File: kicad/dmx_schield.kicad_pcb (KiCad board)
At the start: 2 copper layers, 101.6 x 78.7 mm, 103 parts, among them J1 Conn_01x17, J2 Conn_01x17, J250 Conn_01x01, J251 Conn_01x01, J30 Conn_01x04, J40 Conn_01x06, J41 Conn_01x01, J42 Conn_01x01, J43 Conn_01x01, J50 Conn_01x02, J60 Conn_01x03, Q1 BSR14, Q50 IRLML5203, SW1 SW_Push, SW2 SW_Push, SW3 SW_Push, SW4 SW_Push, U1 DCDC-SIP8-1-2-(3)-6-7, U11 DCDC-SIP7-1-2-4-6, U140 LM317_3PinPackage, U3 LTV-847S, U5 LTV-827S, U6 ADUM1301, U60 MAX481E, U61 74LVC2G34, U7 REE-0505S/1S7E_0505S1.5UP

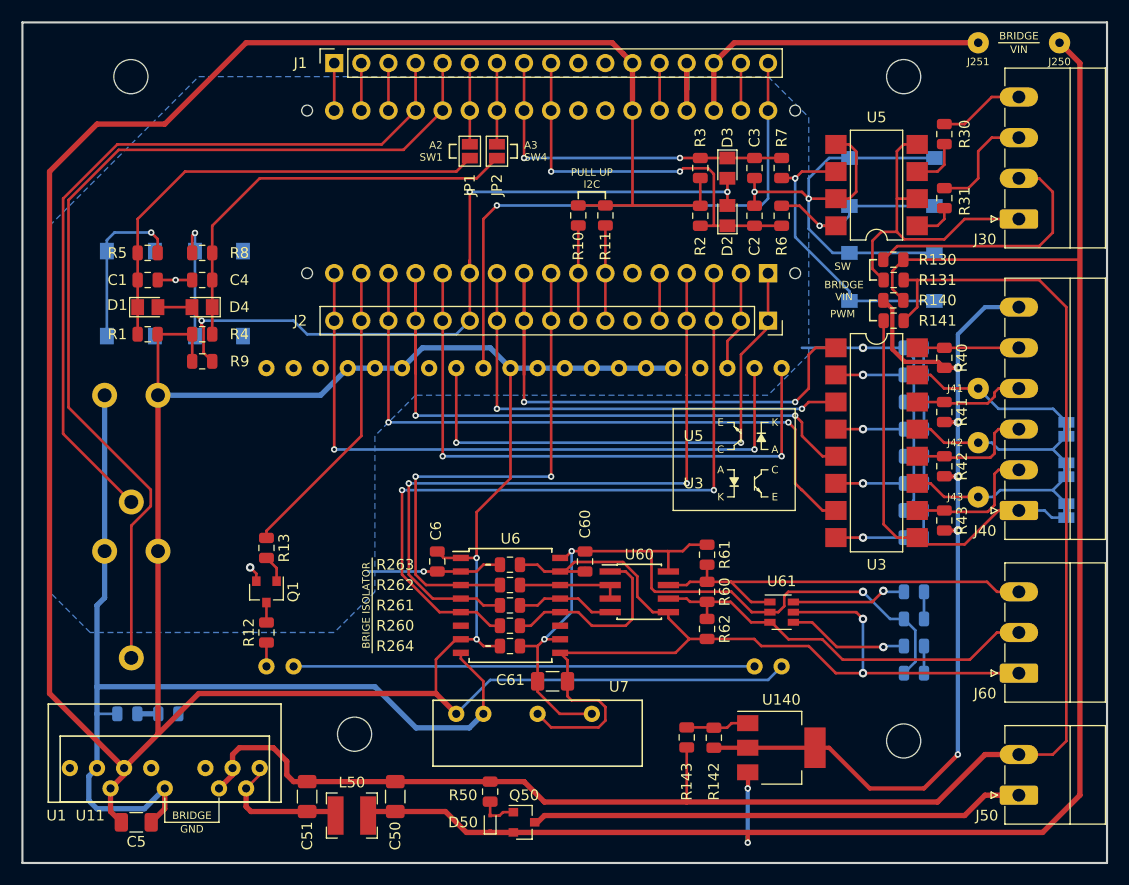
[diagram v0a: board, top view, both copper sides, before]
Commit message: fixed routing errors and error in library
tested is everything, but the DMX circuit and LDO
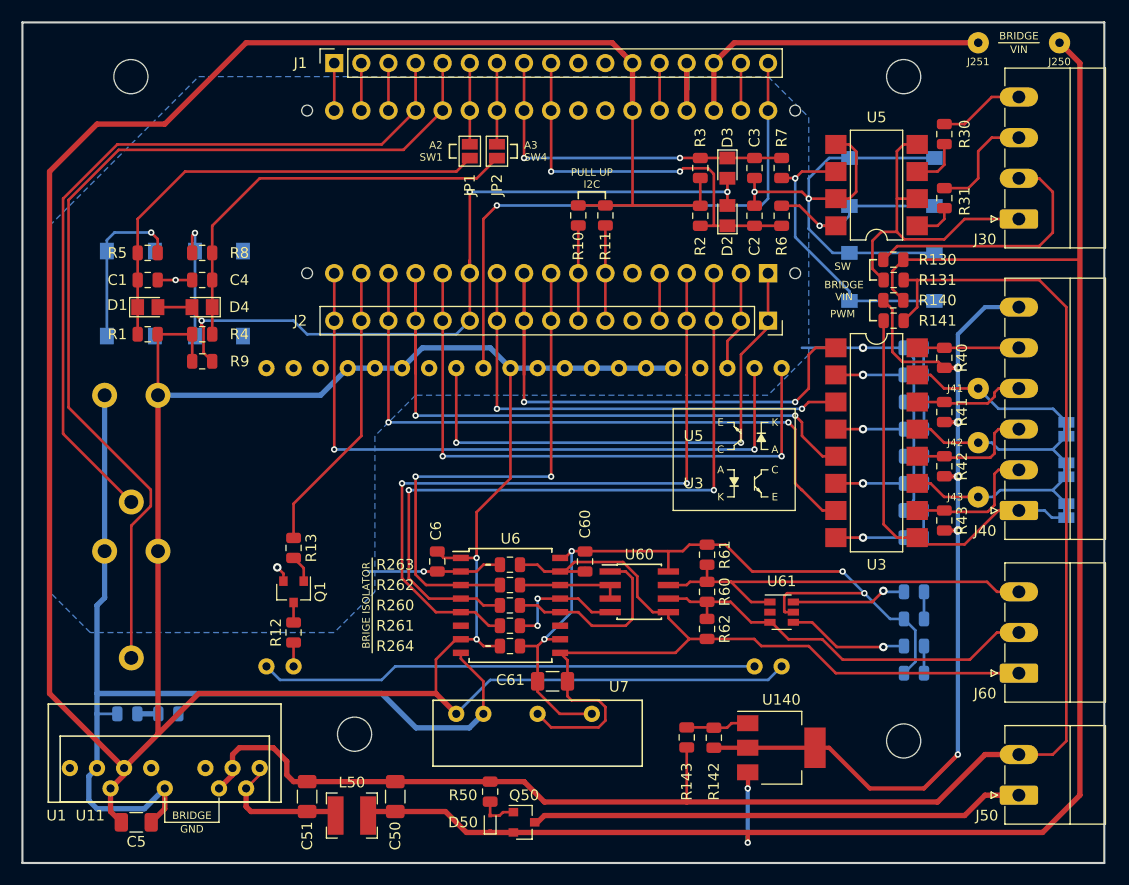
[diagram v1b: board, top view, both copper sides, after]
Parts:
- moved Q1 2.54 mm to (63.5, 142.2)
- moved R12 2.54 mm to (63.5, 146.1)
- moved R13 2.54 mm to (63.5, 138.1)
- moved R261 1.91 mm to (83.8, 145.4)
- moved R260 1.91 mm to (83.8, 143.5)
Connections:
- LCD1 pad 2: Net-(LCD1-Pad19) -> Net-(LCD1-Pad2)
- LCD1 pad 20: Net-(LCD1-Pad20) -> Net-(LCD1-Pad2)
- R12 pad 1: Net-(LCD1-Pad20) -> Net-(LCD1-Pad19)
- U6 pad 4: /RX -> /TX
- U6 pad 5: /TX -> /RX
- U61 pad 2: /60_VCC -> /60_GND
- U61 pad 5: /60_GND -> /60_VCC
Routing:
- net Net-(LCD1-Pad2): track 0.00 -> 46.8 mm
- net Net-(LCD1-Pad19): track 43.2 -> 2.24 mm
- net /60_GND: track 97.6 -> 85.7 mm, vias 2 -> 0
- net Net-(R261-Pad1): track 9.24 -> 11.5 mm, vias 0 -> 2
- net /RX: track 64.0 -> 66.3 mm
- net Net-(LCD1-Pad20): track 2.24 -> 0.00 mm
- net /TX: track 68.6 -> 66.7 mm
- net /BLED: track 28.5 -> 27.4 mm
- net /60_VCC: track 76.2 -> 77.0 mm, vias 3 -> 4
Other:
- board size 101.6 x 78.7 mm -> 101.3 x 78.7 mm
- board text added: "V2.0-Rev1-14/05/2020"
- board text removed: "V2.0-03/05/2020"
